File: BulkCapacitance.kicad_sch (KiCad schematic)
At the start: 4 parts

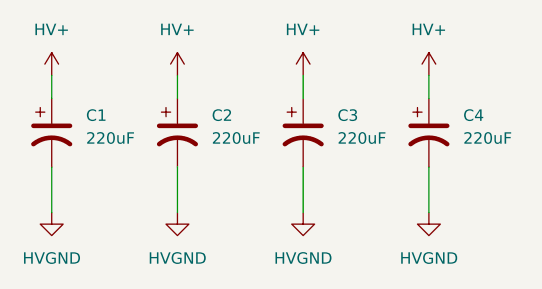
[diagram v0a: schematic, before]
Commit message: killed testpoints
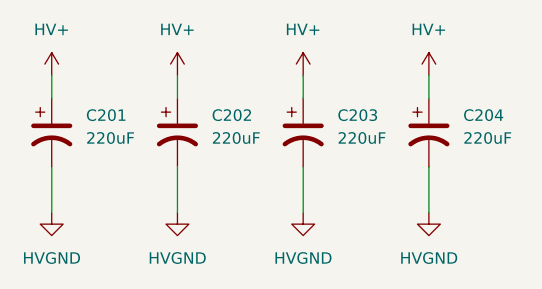
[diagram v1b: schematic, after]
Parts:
- renumbered C1 to C201, C2 to C202, C3 to C203, C4 to C204
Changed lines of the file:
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@@
 		(dnp no)
 		(fields_autoplaced yes)
-		(property "Reference" "#PWR09"
+		(property "Reference" "#PWR0271"
 			(at 153.67 99.06 0)
 			(effects
@@
 			(project "TractionInverter"
 				(path "/bc91ffbf-afc6-42bb-9d28-6a3fecc21fcc/9f0263c3-ed48-4eb7-bb74-b6c123317857"
-					(reference "#PWR09")
+					(reference "#PWR0271")
 					(unit 1)
 				)
@@
 		(dnp no)
 		(fields_autoplaced yes)
-		(property "Reference" "#PWR04"
+		(property "Reference" "#PWR0266"
 			(at 139.7 81.28 0)
 			(effects
@@
 			(project "TractionInverter"
 				(path "/bc91ffbf-afc6-42bb-9d28-6a3fecc21fcc/9f0263c3-ed48-4eb7-bb74-b6c123317857"
-					(reference "#PWR04")
+					(reference "#PWR0266")
 					(unit 1)
 				)
@@
 		(dnp no)
 		(fields_autoplaced yes)
-		(property "Reference" "C1"
+		(property "Reference" "C201"
 			(at 129.54 81.9149 0)
 			(effects
@@
 			(project "TractionInverter"
 				(path "/bc91ffbf-afc6-42bb-9d28-6a3fecc21fcc/9f0263c3-ed48-4eb7-bb74-b6c123317857"
-					(reference "C1")
+					(reference "C201")
 					(unit 1)
 				)
@@
 		(dnp no)
 		(fields_autoplaced yes)
-		(property "Reference" "#PWR08"
+		(property "Reference" "#PWR0270"
 			(at 139.7 99.06 0)
 			(effects
@@
 			(project "TractionInverter"
 				(path "/bc91ffbf-afc6-42bb-9d28-6a3fecc21fcc/9f0263c3-ed48-4eb7-bb74-b6c123317857"
-					(reference "#PWR08")
+					(reference "#PWR0270")
 					(unit 1)
 				)
@@
 		(dnp no)
 		(fields_autoplaced yes)
-		(property "Reference" "#PWR05"
+		(property "Reference" "#PWR0267"
 			(at 153.67 81.28 0)
 			(effects
@@
 			(project "TractionInverter"
 				(path "/bc91ffbf-afc6-42bb-9d28-6a3fecc21fcc/9f0263c3-ed48-4eb7-bb74-b6c123317857"
-					(reference "#PWR05")
+					(reference "#PWR0267")
 					(unit 1)
 				)
@@
 		(dnp no)
 		(fields_autoplaced yes)
-		(property "Reference" "#PWR010"
+		(property "Reference" "#PWR0272"
 			(at 167.64 99.06 0)
 			(effects
@@
 			(project "TractionInverter"
 				(path "/bc91ffbf-afc6-42bb-9d28-6a3fecc21fcc/9f0263c3-ed48-4eb7-bb74-b6c123317857"
-					(reference "#PWR010")
+					(reference "#PWR0272")
 					(unit 1)
 				)
@@
 		(dnp no)
 		(fields_autoplaced yes)
-		(property "Reference" "C2"
+		(property "Reference" "C202"
 			(at 143.51 81.9149 0)
 			(effects
@@
 			(project "TractionInverter"
 				(path "/bc91ffbf-afc6-42bb-9d28-6a3fecc21fcc/9f0263c3-ed48-4eb7-bb74-b6c123317857"
-					(reference "C2")
+					(reference "C202")
 					(unit 1)
 				)
@@
 		(dnp no)
 		(fields_autoplaced yes)
-		(property "Reference" "#PWR06"
+		(property "Reference" "#PWR0268"
 			(at 167.64 81.28 0)
 			(effects
@@
 			(project "TractionInverter"
 				(path "/bc91ffbf-afc6-42bb-9d28-6a3fecc21fcc/9f0263c3-ed48-4eb7-bb74-b6c123317857"
-					(reference "#PWR06")
+					(reference "#PWR0268")
 					(unit 1)
 				)
@@
 		(dnp no)
 		(fields_autoplaced yes)
-		(property "Reference" "C4"
+		(property "Reference" "C204"
 			(at 171.45 81.9149 0)
 			(effects
@@
 			(project "TractionInverter"
 				(path "/bc91ffbf-afc6-42bb-9d28-6a3fecc21fcc/9f0263c3-ed48-4eb7-bb74-b6c123317857"
-					(reference "C4")
+					(reference "C204")
 					(unit 1)
 				)
@@
 		(dnp no)
 		(fields_autoplaced yes)
-		(property "Reference" "#PWR07"
+		(property "Reference" "#PWR0269"
 			(at 125.73 99.06 0)
 			(effects
@@
 			(project "TractionInverter"
 				(path "/bc91ffbf-afc6-42bb-9d28-6a3fecc21fcc/9f0263c3-ed48-4eb7-bb74-b6c123317857"
-					(reference "#PWR07")
+					(reference "#PWR0269")
 					(unit 1)
 				)
@@
 		(dnp no)
 		(fields_autoplaced yes)
-		(property "Reference" "C3"
+		(property "Reference" "C203"
 			(at 157.48 81.9149 0)
 			(effects
@@
 			(project "TractionInverter"
 				(path "/bc91ffbf-afc6-42bb-9d28-6a3fecc21fcc/9f0263c3-ed48-4eb7-bb74-b6c123317857"
-					(reference "C3")
+					(reference "C203")
 					(unit 1)
 				)
@@
 		(dnp no)
 		(fields_autoplaced yes)
-		(property "Reference" "#PWR03"
+		(property "Reference" "#PWR0265"
 			(at 125.73 81.28 0)
 			(effects
@@
 			(project "TractionInverter"
 				(path "/bc91ffbf-afc6-42bb-9d28-6a3fecc21fcc/9f0263c3-ed48-4eb7-bb74-b6c123317857"
-					(reference "#PWR03")
-					(unit 1)
-				)
+					(reference "#PWR0265")
+					(unit 1)
+				)
